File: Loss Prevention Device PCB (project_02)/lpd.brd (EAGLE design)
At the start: 160 x 100 mm, 0 parts

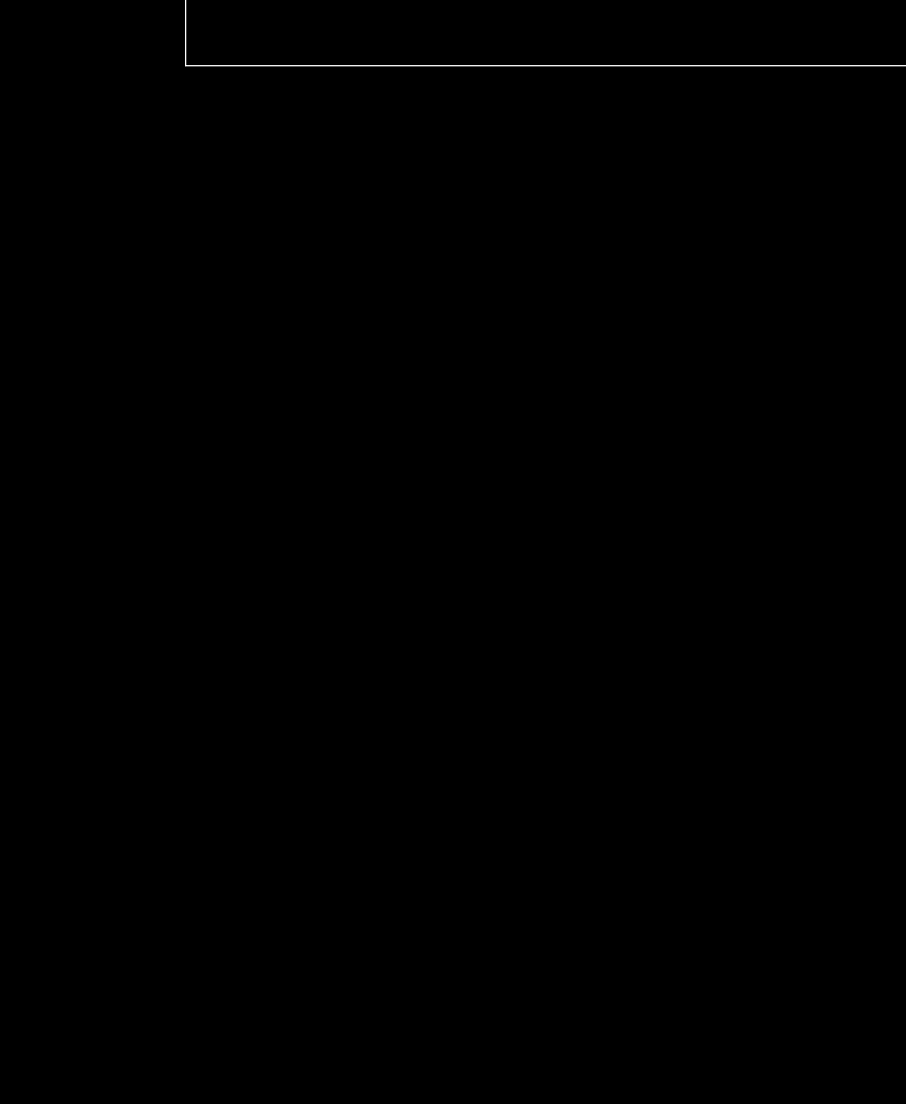
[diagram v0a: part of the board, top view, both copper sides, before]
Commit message: Schematic'ed all parts but the usb
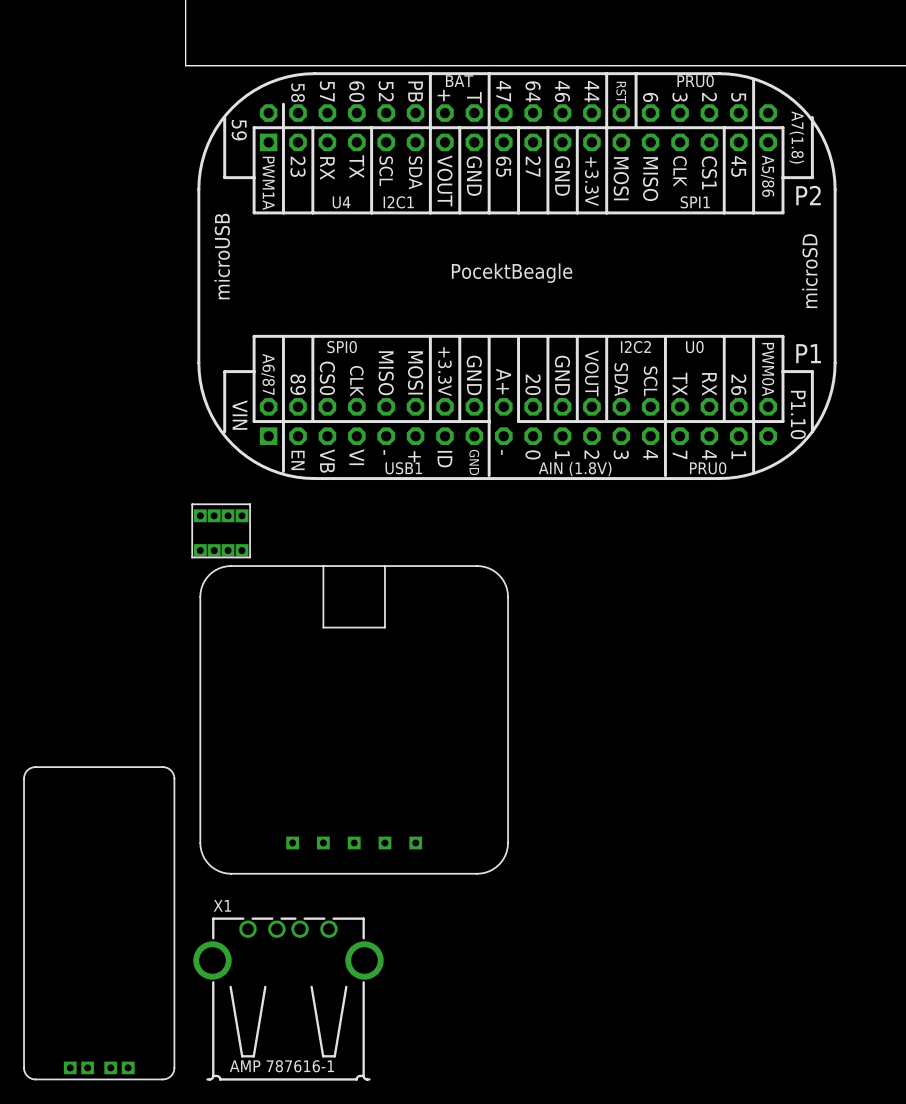
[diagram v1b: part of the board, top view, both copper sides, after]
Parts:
- added K1: LPPB041NGCN-RC, lpd:FEMALE90
- added U1: POCKETBEAGLE, lpd:POCKETBEAGLE
- added U2: GT-U7, lpd:GPS
- added U3: HM-10, lpd:BT
- added X1: (no value), lpd:GHI2_USB_HOST_HORIZONTAL_W/CHASSIS_GND
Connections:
- new net ANGLE1: K1.P$5, U3.P$4
- new net ANGLE2: K1.P$6, U3.P$1
- new net ANGLE3: K1.P$7, U3.P$3
- new net ANGLE4: K1.P$8, U3.P$2
- new net BAT.VIN: U1.P2_14
- new net GND: K1.P$2, U1.P1_16, U1.P1_22, U1.P2_15, U1.P2_21, U2.P$1
- new net UART2.RX: U1.P1_08, U2.P$3
- new net UART2.TX: U1.P1_10, U2.P$4
- new net UART4.RX: K1.P$4, U1.P2_05
- new net UART4.TX: K1.P$3, U1.P2_07
- new net VDD_3P3V: K1.P$1, U1.P1_14, U1.P2_23, U2.P$5
- new net VIN: U1.P1_01
- new net VOUT: U1.P1_24, U1.P2_13
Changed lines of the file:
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@@
 </autorouter>
 <elements>
+<element name="U1" library="lpd" package="POCKETBEAGLE" value="POCKETBEAGLE" x="1.27" y="-35.56" smashed="yes"/>
+<element name="K1" library="lpd" package="FEMALE90" value="LPPB041NGCN-RC" x="1.27" y="-41.91" smashed="yes"/>
+<element name="U2" library="lpd" package="GPS" value="GT-U7" x="1.27" y="-69.85" smashed="yes"/>
+<element name="X1" library="lpd" package="GHI2_USB_HOST_HORIZONTAL_W/CHASSIS_GND" value="" x="8.89" y="-87.63" smashed="yes">
+<attribute name="NAME" x="2.3899" y="-73.1299" size="1.016" layer="25" ratio="12"/>
+<attribute name="VALUE" x="4.3899" y="-77.63" size="1.016" layer="27" ratio="12"/>
+</element>
+<element name="U3" library="lpd" package="BT" value="HM-10" x="-13.97" y="-87.63" smashed="yes"/>
 </elements>
 <signals>
+<signal name="VIN">
+<contactref element="U1" pad="P1_01"/>
+</signal>
+<signal name="GND">
+<contactref element="U1" pad="P1_16"/>
+<contactref element="U1" pad="P1_22"/>
+<contactref element="U1" pad="P2_15"/>
+<contactref element="U1" pad="P2_21"/>
+<contactref element="U2" pad="P$1"/>
+<contactref element="K1" pad="P$2"/>
+<wire x1="2.47" y1="-41.91" x2="9.25" y2="-67.19" width="0" layer="19" extent="1-1"/>
+<wire x1="24.96" y1="-29.49" x2="2.47" y2="-41.91" width="0" layer="19" extent="1-1"/>
+<wire x1="32.58" y1="-29.49" x2="24.96" y2="-29.49" width="0" layer="19" extent="1-1"/>
+<wire x1="32.58" y1="-6.63" x2="32.58" y2="-29.49" width="0" layer="19" extent="1-1"/>
+<wire x1="24.96" y1="-6.63" x2="32.58" y2="-6.63" width="0" layer="19" extent="1-1"/>
+</signal>
+<signal name="VOUT">
+<contactref element="U1" pad="P1_24"/>
+<contactref element="U1" pad="P2_13"/>
+<wire x1="35.12" y1="-29.49" x2="22.42" y2="-6.63" width="0" layer="19" extent="1-1"/>
+</signal>
+<signal name="BAT.VIN">
+<contactref element="U1" pad="P2_14"/>
+</signal>
+<signal name="VDD_3P3V">
+<contactref element="U1" pad="P2_23"/>
+<contactref element="U1" pad="P1_14"/>
+<contactref element="U2" pad="P$5"/>
+<contactref element="K1" pad="P$1"/>
+<wire x1="1.27" y1="-41.91" x2="19.89" y2="-67.19" width="0" layer="19" extent="1-1"/>
+<wire x1="22.42" y1="-29.49" x2="1.27" y2="-41.91" width="0" layer="19" extent="1-1"/>
+<wire x1="35.12" y1="-6.63" x2="22.42" y2="-29.49" width="0" layer="19" extent="1-1"/>
+</signal>
+<signal name="UART2.RX">
+<contactref element="U1" pad="P1_08"/>
+<contactref element="U2" pad="P$3"/>
+<wire x1="14.8" y1="-29.49" x2="14.57" y2="-67.19" width="0" layer="19" extent="1-1"/>
+</signal>
+<signal name="UART2.TX">
+<contactref element="U1" pad="P1_10"/>
+<contactref element="U2" pad="P$4"/>
+<wire x1="17.34" y1="-29.49" x2="17.23" y2="-67.19" width="0" layer="19" extent="1-1"/>
+</signal>
+<signal name="UART4.TX">
+<contactref element="U1" pad="P2_07"/>
+<contactref element="K1" pad="P$3"/>
+<wire x1="14.8" y1="-6.63" x2="3.67" y2="-41.91" width="0" layer="19" extent="1-1"/>
+</signal>
+<signal name="UART4.RX">
+<contactref element="U1" pad="P2_05"/>
+<contactref element="K1" pad="P$4"/>
+<wire x1="12.26" y1="-6.63" x2="4.87" y2="-41.91" width="0" layer="19" extent="1-1"/>
+</signal>
+<signal name="ANGLE1">
+<contactref element="K1" pad="P$5"/>
+<contactref element="U3" pad="P$4"/>
+<wire x1="1.27" y1="-38.91" x2="-4.97" y2="-86.63" width="0" layer="19" extent="1-1"/>
+</signal>
+<signal name="ANGLE2">
+<contactref element="K1" pad="P$6"/>
+<contactref element="U3" pad="P$1"/>
+<wire x1="2.47" y1="-38.91" x2="-9.97" y2="-86.63" width="0" layer="19" extent="1-1"/>
+</signal>
+<signal name="ANGLE3">
+<contactref element="K1" pad="P$7"/>
+<contactref element="U3" pad="P$3"/>
+<wire x1="3.67" y1="-38.91" x2="-6.47" y2="-86.63" width="0" layer="19" extent="1-1"/>
+</signal>
+<signal name="ANGLE4">
+<contactref element="K1" pad="P$8"/>
+<contactref element="U3" pad="P$2"/>
+<wire x1="4.87" y1="-38.91" x2="-8.47" y2="-86.63" width="0" layer="19" extent="1-1"/>
+</signal>
 </signals>
 <mfgpreviewcolors>

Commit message: Added USB connections
For some reason when I imported the CGND part to my LPD library my schematic couldn't read from it anymore...
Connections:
- new net CGND: X1.5, X1.6
- new net USB1.D+: U1.P1_11, X1.3
- new net USB1.D-: U1.P1_09, X1.2
- new net USB1.GND: X1.4
- new net USB1.VBUS: U1.P1_05, X1.1
- net GND: now also U1.P1_15
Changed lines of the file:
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@@
 <contactref element="U2" pad="P$1"/>
 <contactref element="K1" pad="P$2"/>
+<contactref element="U1" pad="P1_15"/>
 <wire x1="2.47" y1="-41.91" x2="9.25" y2="-67.19" width="0" layer="19" extent="1-1"/>
-<wire x1="24.96" y1="-29.49" x2="2.47" y2="-41.91" width="0" layer="19" extent="1-1"/>
+<wire x1="24.96" y1="-32.03" x2="2.47" y2="-41.91" width="0" layer="19" extent="1-1"/>
+<wire x1="24.96" y1="-29.49" x2="24.96" y2="-32.03" width="0" layer="19" extent="1-1"/>
 <wire x1="32.58" y1="-29.49" x2="24.96" y2="-29.49" width="0" layer="19" extent="1-1"/>
 <wire x1="32.58" y1="-6.63" x2="32.58" y2="-29.49" width="0" layer="19" extent="1-1"/>
@@
 <wire x1="4.87" y1="-38.91" x2="-8.47" y2="-86.63" width="0" layer="19" extent="1-1"/>
 </signal>
+<signal name="CGND">
+<contactref element="X1" pad="5"/>
+<contactref element="X1" pad="6"/>
+<wire x1="15.46" y1="-77.3501" x2="2.32" y2="-77.3501" width="0" layer="19" extent="1-1"/>
+</signal>
+<signal name="USB1.VBUS">
+<contactref element="X1" pad="1"/>
+<contactref element="U1" pad="P1_05"/>
+<wire x1="12.26" y1="-32.03" x2="5.39" y2="-74.64" width="0" layer="19" extent="1-1"/>
+</signal>
+<signal name="USB1.D-">
+<contactref element="X1" pad="2"/>
+<contactref element="U1" pad="P1_09"/>
+<wire x1="17.34" y1="-32.03" x2="7.89" y2="-74.64" width="0" layer="19" extent="1-1"/>
+</signal>
+<signal name="USB1.D+">
+<contactref element="X1" pad="3"/>
+<contactref element="U1" pad="P1_11"/>
+<wire x1="19.88" y1="-32.03" x2="9.89" y2="-74.64" width="0" layer="19" extent="1-1"/>
+</signal>
+<signal name="USB1.GND">
+<contactref element="X1" pad="4"/>
+</signal>
 </signals>

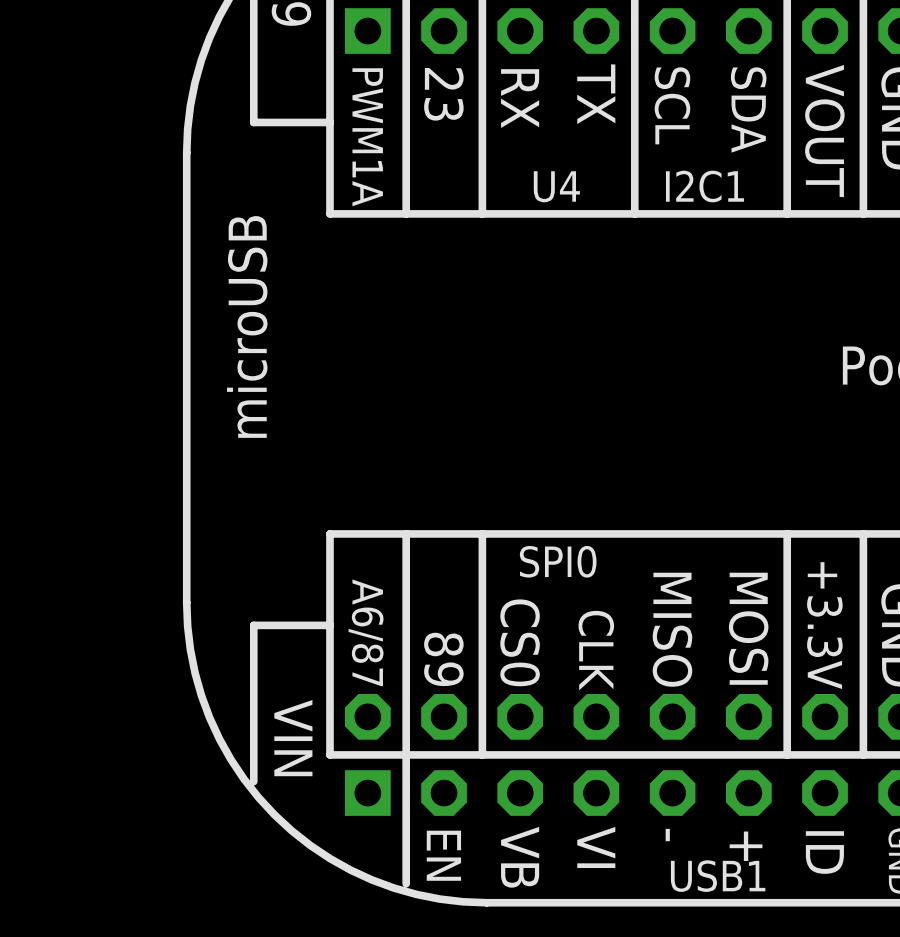
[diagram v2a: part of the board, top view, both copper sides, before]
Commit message: Updated PocketBeagle Symbol/Footprint
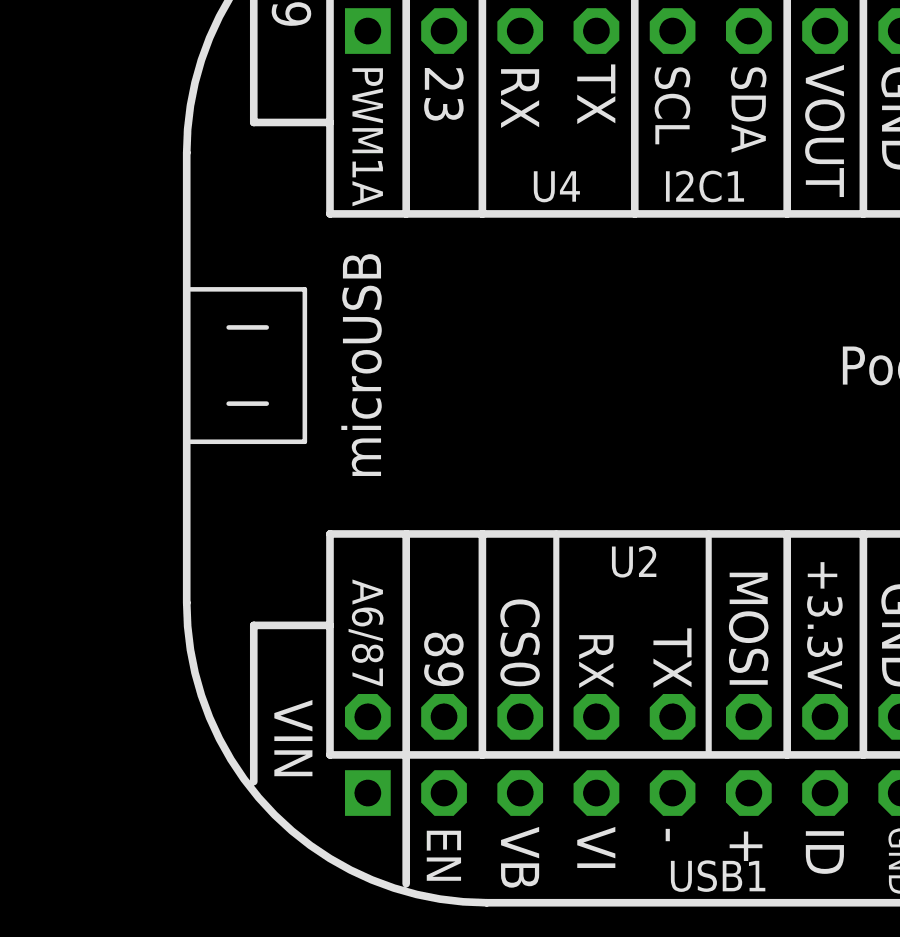
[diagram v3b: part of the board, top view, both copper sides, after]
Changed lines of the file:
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@@
 </signal>
 <signal name="GND">
-<contactref element="U1" pad="P1_16"/>
 <contactref element="U1" pad="P1_22"/>
-<contactref element="U1" pad="P2_15"/>
 <contactref element="U1" pad="P2_21"/>
 <contactref element="U2" pad="P$1"/>
 <contactref element="K1" pad="P$2"/>
 <contactref element="U1" pad="P1_15"/>
+<contactref element="U1" pad="P1_16"/>
+<contactref element="U1" pad="P2_15"/>
 <wire x1="2.47" y1="-41.91" x2="9.25" y2="-67.19" width="0" layer="19" extent="1-1"/>
 <wire x1="24.96" y1="-32.03" x2="2.47" y2="-41.91" width="0" layer="19" extent="1-1"/>
@@
 </signal>
 <signal name="UART2.RX">
+<contactref element="U2" pad="P$3"/>
 <contactref element="U1" pad="P1_08"/>
-<contactref element="U2" pad="P$3"/>
 <wire x1="14.8" y1="-29.49" x2="14.57" y2="-67.19" width="0" layer="19" extent="1-1"/>
 </signal>
 <signal name="UART2.TX">
+<contactref element="U2" pad="P$4"/>
 <contactref element="U1" pad="P1_10"/>
-<contactref element="U2" pad="P$4"/>
 <wire x1="17.34" y1="-29.49" x2="17.23" y2="-67.19" width="0" layer="19" extent="1-1"/>
 </signal>
 <signal name="UART4.TX">
+<contactref element="K1" pad="P$3"/>
 <contactref element="U1" pad="P2_07"/>
-<contactref element="K1" pad="P$3"/>
 <wire x1="14.8" y1="-6.63" x2="3.67" y2="-41.91" width="0" layer="19" extent="1-1"/>
 </signal>
 <signal name="UART4.RX">
+<contactref element="K1" pad="P$4"/>
 <contactref element="U1" pad="P2_05"/>
-<contactref element="K1" pad="P$4"/>
 <wire x1="12.26" y1="-6.63" x2="4.87" y2="-41.91" width="0" layer="19" extent="1-1"/>
 </signal>
